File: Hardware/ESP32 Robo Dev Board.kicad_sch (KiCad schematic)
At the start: 44 parts, among them J2 Conn_01x02_Pin, Q1 DMP2045U, SW1 SW_Push_Dual_x2, U1 ESP32-S3-WROOM-1, U2 TCA9548ARGER, U8 MCP73831-2-OT, U9 AP2112K-3.3

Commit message: Tweaked n' fixed things with @Amoskeag
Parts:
- added Rs2: 18 KΩ, Resistor_SMD:R_0603_1608Metric, symbol Device:R_Small
- added Rs3: 100, Resistor_SMD:R_0603_1608Metric, symbol Device:R_Small
- added SW2: SW_Push, Button_Switch_THT:SW_TH_Tactile_Omron_B3F-100x, symbol Switch:SW_Push
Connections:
- net +3V3: now also Rs3.2
- net Boot: now also Rs2.2, SW2.2
- net GND: now also Rs2.1
- new net: Rs3.1, SW2.1

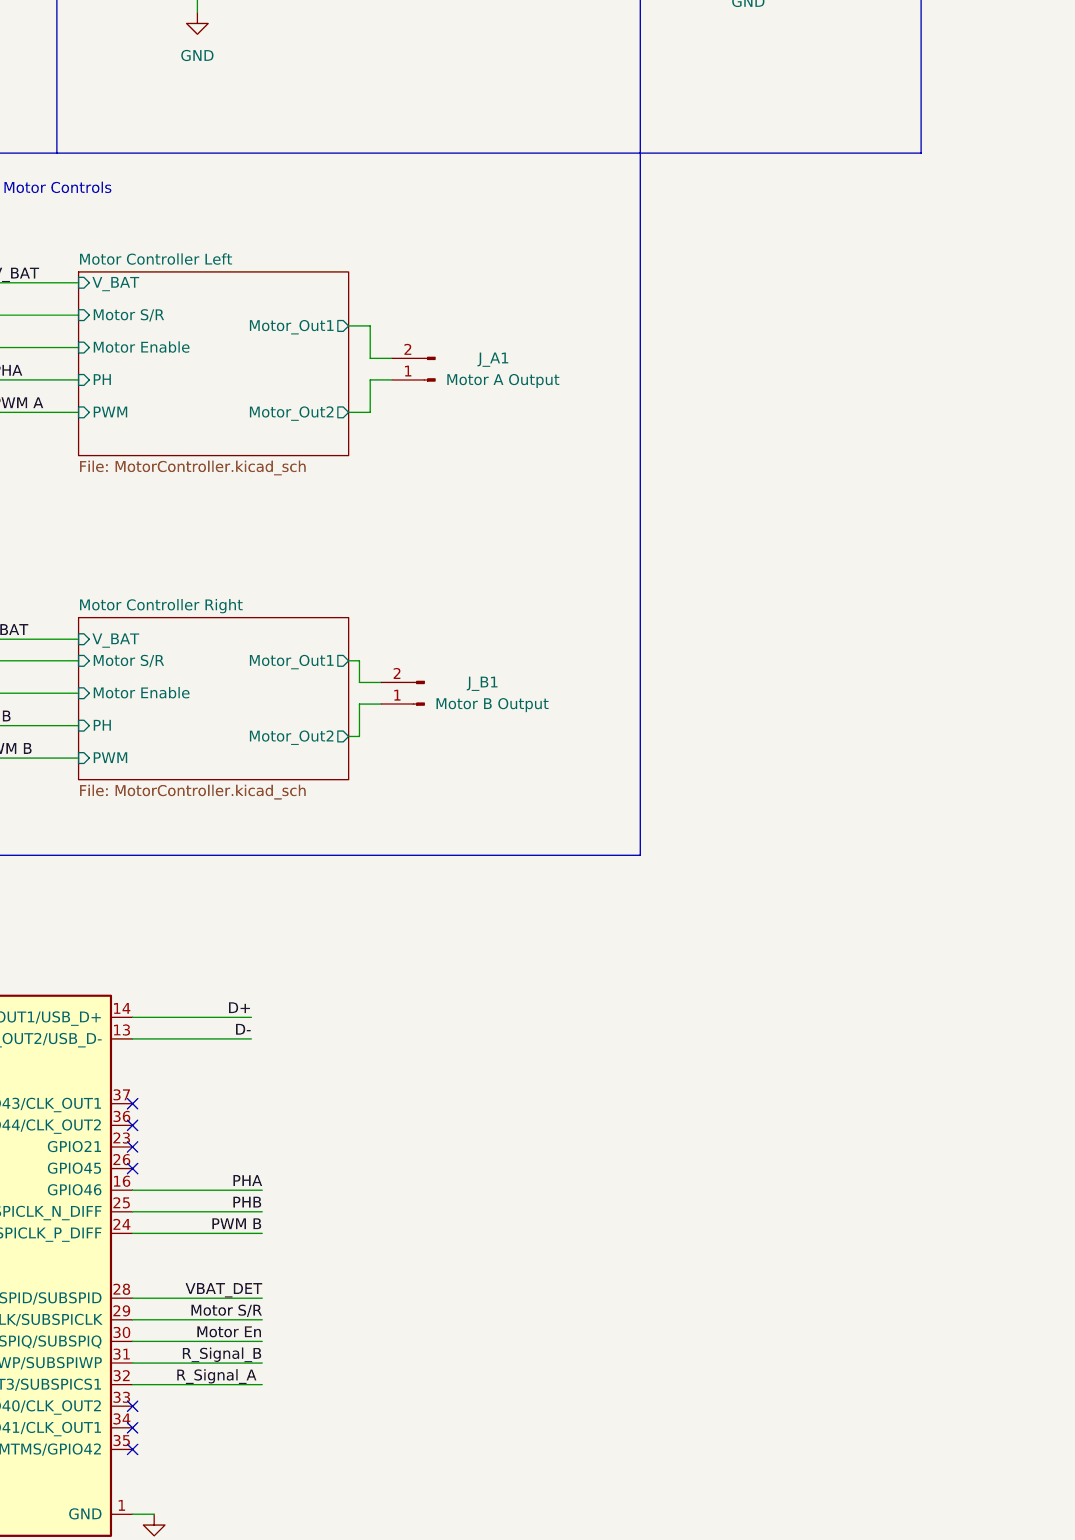
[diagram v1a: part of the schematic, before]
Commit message: Add JST Connectors for Encoders
Added JST Connectors for my Encoders to attach to.

Fixed all DRC Errors.
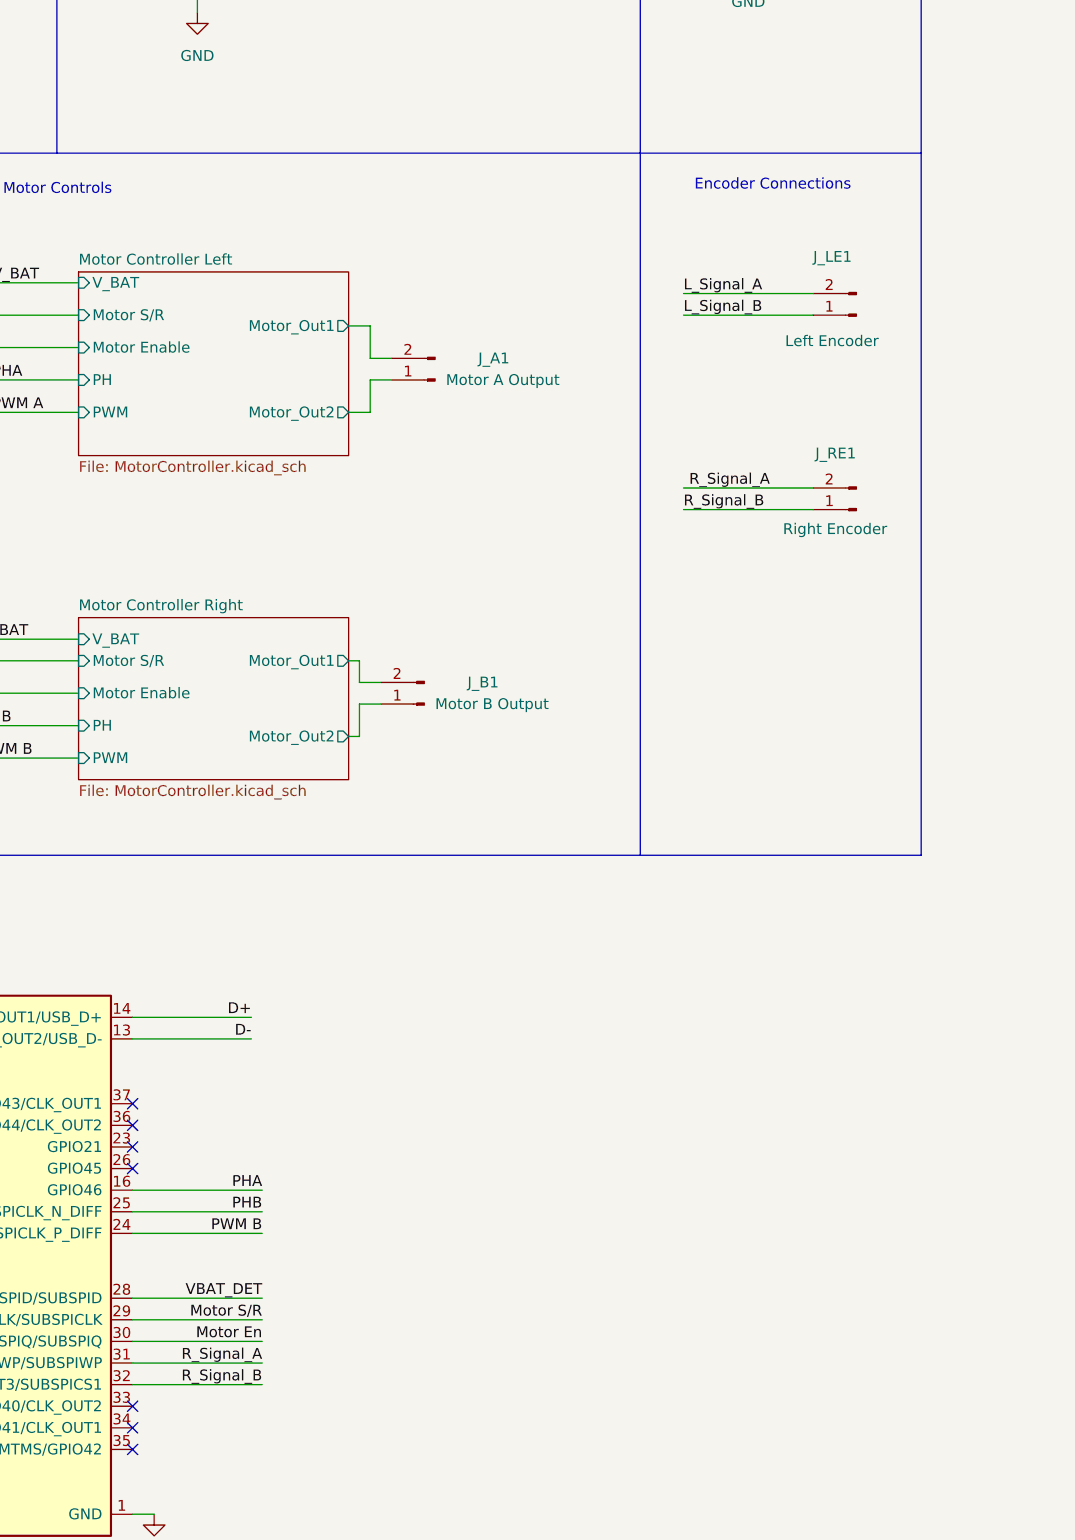
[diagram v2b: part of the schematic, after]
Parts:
- added J_LE1: Left Encoder, Connector_JST:JST_EH_B2B-EH-A_1x02_P2.50mm_Vertical, symbol Connector:Conn_01x02_Male
- added J_RE1: Right Encoder, Connector_JST:JST_EH_B2B-EH-A_1x02_P2.50mm_Vertical, symbol Connector:Conn_01x02_Male
- SW1: footprint Button_Switch_SMD:SW_Push_SPST_NO_Alps_SKRK -> Button_Switch_THT:SW_TH_Tactile_Omron_B3F-100x
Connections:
- net L_Signal_A: now also J_LE1.2 (Pin_2)
- net L_Signal_B: now also J_LE1.1 (Pin_1)
- net R_Signal_A: now also U1.31 (GPIO38/FSPIWP/SUBSPIWP), J_RE1.2 (Pin_2); no longer U1.32 (MTCK/GPIO39/CLK_OUT3/SUBSPICS1)
- net R_Signal_B: now also U1.32 (MTCK/GPIO39/CLK_OUT3/SUBSPICS1), J_RE1.1 (Pin_1); no longer U1.31 (GPIO38/FSPIWP/SUBSPIWP)
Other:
- note added: "Encoder Connections"
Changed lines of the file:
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@@
 		)
 	)
+	(text "Encoder Connections\n"
+		(exclude_from_sim no)
+		(at 322.58 82.042 0)
+		(effects
+			(font
+				(size 1.27 1.27)
+			)
+			(justify left bottom)
+		)
+	)
 	(text "Reset Circuts"
 		(exclude_from_sim no)
@@
 		)
 	)
+	(polyline
+		(pts
+			(xy 316.23 160.02) (xy 349.25 160.02)
+		)
+		(stroke
+			(width 0)
+			(type default)
+		)
+	)
 	(wire
 		(pts
@@
 		)
 	)
+	(polyline
+		(pts
+			(xy 349.25 77.47) (xy 349.25 160.02)
+		)
+		(stroke
+			(width 0)
+			(type default)
+		)
+	)
 	(wire
 		(pts
@@
 	(wire
 		(pts
-			(xy 256.54 222.25) (xy 271.78 222.25)
-		)
-		(stroke
-			(width 0)
-			(type default)
-		)
-	)
-	(wire
-		(pts
 			(xy 140.97 53.34) (xy 140.97 55.88)
 		)
@@
 	(wire
 		(pts
+			(xy 321.31 96.52) (xy 336.55 96.52)
+		)
+		(stroke
+			(width 0)
+			(type default)
+		)
+	)
+	(wire
+		(pts
 			(xy 26.67 114.3) (xy 21.59 114.3)
 		)
@@
 	(wire
 		(pts
+			(xy 336.55 116.84) (xy 321.31 116.84)
+		)
+		(stroke
+			(width 0)
+			(type default)
+		)
+	)
+	(wire
+		(pts
 			(xy 240.03 107.95) (xy 250.19 107.95)
 		)
@@
 	(wire
 		(pts
+			(xy 336.55 119.38) (xy 321.31 119.38)
+		)
+		(stroke
+			(width 0)
+			(type default)
+		)
+	)
+	(wire
+		(pts
 			(xy 57.15 90.17) (xy 58.42 90.17)
 		)
@@
 	(wire
 		(pts
-			(xy 256.54 199.39) (xy 271.78 199.39)
+			(xy 256.54 219.71) (xy 271.78 219.71)
 		)
 		(stroke
@@
 	(wire
 		(pts
-			(xy 147.32 127) (xy 166.37 127)
+			(xy 256.54 199.39) (xy 271.78 199.39)
 		)
 		(stroke
@@
 	(wire
 		(pts
-			(xy 284.48 104.14) (xy 287.02 104.14)
+			(xy 147.32 127) (xy 166.37 127)
 		)
 		(stroke
@@
 	(wire
 		(pts
-			(xy 267.97 46.99) (xy 267.97 57.15)
+			(xy 284.48 104.14) (xy 287.02 104.14)
 		)
 		(stroke
@@
 	(wire
 		(pts
-			(xy 127 217.17) (xy 142.24 217.17)
+			(xy 267.97 46.99) (xy 267.97 57.15)
 		)
 		(stroke
@@
 	(wire
 		(pts
-			(xy 256.54 219.71) (xy 271.78 219.71)
+			(xy 127 217.17) (xy 142.24 217.17)
 		)
 		(stroke
@@
 	(wire
 		(pts
+			(xy 256.54 222.25) (xy 271.78 222.25)
+		)
+		(stroke
+			(width 0)
+			(type default)
+		)
+	)
+	(wire
+		(pts
 			(xy 124.46 67.31) (xy 124.46 26.67)
 		)
@@
 	(wire
 		(pts
+			(xy 321.31 93.98) (xy 336.55 93.98)
+		)
+		(stroke
+			(width 0)
+			(type default)
+		)
+	)
+	(wire
+		(pts
 			(xy 82.55 156.21) (xy 80.01 156.21)
 		)
@@
 	)
 	(label "R_Signal_B"
-		(at 271.78 219.71 180)
+		(at 271.78 222.25 180)
 		(effects
 			(font
@@
 		)
 	)
+	(label "R_Signal_B"
+		(at 321.31 119.38 0)
+		(effects
+			(font
+				(size 1.27 1.27)
+			)
+			(justify left bottom)
+		)
+	)
 	(label "I2C_1D"
 		(at 156.21 106.68 180)
@@
 		)
 	)
+	(label "L_Signal_B"
+		(at 321.31 96.52 0)
+		(effects
+			(font
+				(size 1.27 1.27)
+			)
+			(justify left bottom)
+		)
+	)
 	(label "I2C_5C"
 		(at 82.55 111.76 180)
@@
 		)
 	)
+	(label "R_Signal_A"
+		(at 331.47 116.84 180)
+		(effects
+			(font
+				(size 1.27 1.27)
+			)
+			(justify right bottom)
+		)
+	)
 	(label "I2C_3C"
 		(at 60.96 158.75 180)
@@
 		)
 	)
+	(label "L_Signal_A"
+		(at 321.31 93.98 0)
+		(effects
+			(font
+				(size 1.27 1.27)
+			)
+			(justify left bottom)
+		)
+	)
 	(label "V_IN"
 		(at 50.8 40.64 0)
@@
 	)
 	(label "R_Signal_A"
-		(at 261.62 222.25 0)
+		(at 271.78 219.71 180)
 		(effects
 			(font
 				(size 1.27 1.27)
 			)
-			(justify left bottom)
+			(justify right bottom)
 		)
 	)
@@
 	)
 	(symbol
+		(lib_id "Connector:Conn_01x02_Male")
+		(at 341.63 96.52 180)
+		(unit 1)
+		(exclude_from_sim no)
+		(in_bom yes)
+		(on_board yes)
+		(dnp no)
+		(property "Reference" "J_LE1"
+			(at 336.55 89.662 0)
+			(effects
+				(font
+					(size 1.27 1.27)
+				)
+				(justify right)
+			)
+		)
+		(property "Value" "Left Encoder"
+			(at 333.248 99.568 0)
+			(effects
+				(font
+					(size 1.27 1.27)
+				)
+				(justify right)
+			)
+		)
+		(property "Footprint" "Connector_JST:JST_EH_B2B-EH-A_1x02_P2.50mm_Vertical"
+			(at 341.63 96.52 0)
+			(effects
+				(font
+					(size 1.27 1.27)
+				)
+				(hide yes)
+			)
+		)
+		(property "Datasheet" "~"
+			(at 341.63 96.52 0)
+			(effects
+				(font
+					(size 1.27 1.27)
+				)
+				(hide yes)
+			)
+		)
+		(property "Description" ""
+			(at 341.63 96.52 0)
+			(effects
+				(font
+					(size 1.27 1.27)
+				)
+				(hide yes)
+			)
+		)
+		(pin "1"
+		)
+		(pin "2"
+		)
+		(instances
+			(project "ESP32 Robo Dev Board"
+				(path "/e63e39d7-6ac0-4ffd-8aa3-1841a4541b55"
+					(reference "J_LE1")
+					(unit 1)
+				)
+			)
+		)
+	)
+	(symbol
 		(lib_id "power:GND")
 		(at 88.9 207.01 0)
@@
 	)
 	(symbol
+		(lib_id "Connector:Conn_01x02_Male")
+		(at 341.63 119.38 180)
+		(unit 1)
+		(exclude_from_sim no)
+		(in_bom yes)
+		(on_board yes)
+		(dnp no)
+		(property "Reference" "J_RE1"
+			(at 336.804 112.776 0)
+			(effects
+				(font
+					(size 1.27 1.27)
+				)
+				(justify right)
+			)
+		)
+		(property "Value" "Right Encoder"
+			(at 332.994 121.666 0)
+			(effects
+				(font
+					(size 1.27 1.27)
+				)
+				(justify right)
+			)
+		)
+		(property "Footprint" "Connector_JST:JST_EH_B2B-EH-A_1x02_P2.50mm_Vertical"
+			(at 341.63 119.38 0)
+			(effects
+				(font
+					(size 1.27 1.27)
+				)
+				(hide yes)
+			)
+		)
+		(property "Datasheet" "~"
+			(at 341.63 119.38 0)
+			(effects
+				(font
+					(size 1.27 1.27)
+				)
+				(hide yes)
+			)
+		)
+		(property "Description" ""
+			(at 341.63 119.38 0)
+			(effects
+				(font
+					(size 1.27 1.27)
+				)
+				(hide yes)
+			)
+		)
+		(pin "1"
+		)
+		(pin "2"
+		)
+		(instances
+			(project "ESP32 Robo Dev Board"
+				(path "/e63e39d7-6ac0-4ffd-8aa3-1841a4541b55"
+					(reference "J_RE1")
+					(unit 1)
+				)
+			)
+		)
+	)
+	(symbol
 		(lib_id "Device:R_Small")
 		(at 220.98 49.53 0)
@@
 			)
 		)
-		(property "Footprint" "Button_Switch_SMD:SW_Push_SPST_NO_Alps_SKRK"
+		(property "Footprint" "Button_Switch_THT:SW_TH_Tactile_Omron_B3F-100x"
 			(at 254 44.45 0)
 			(effects

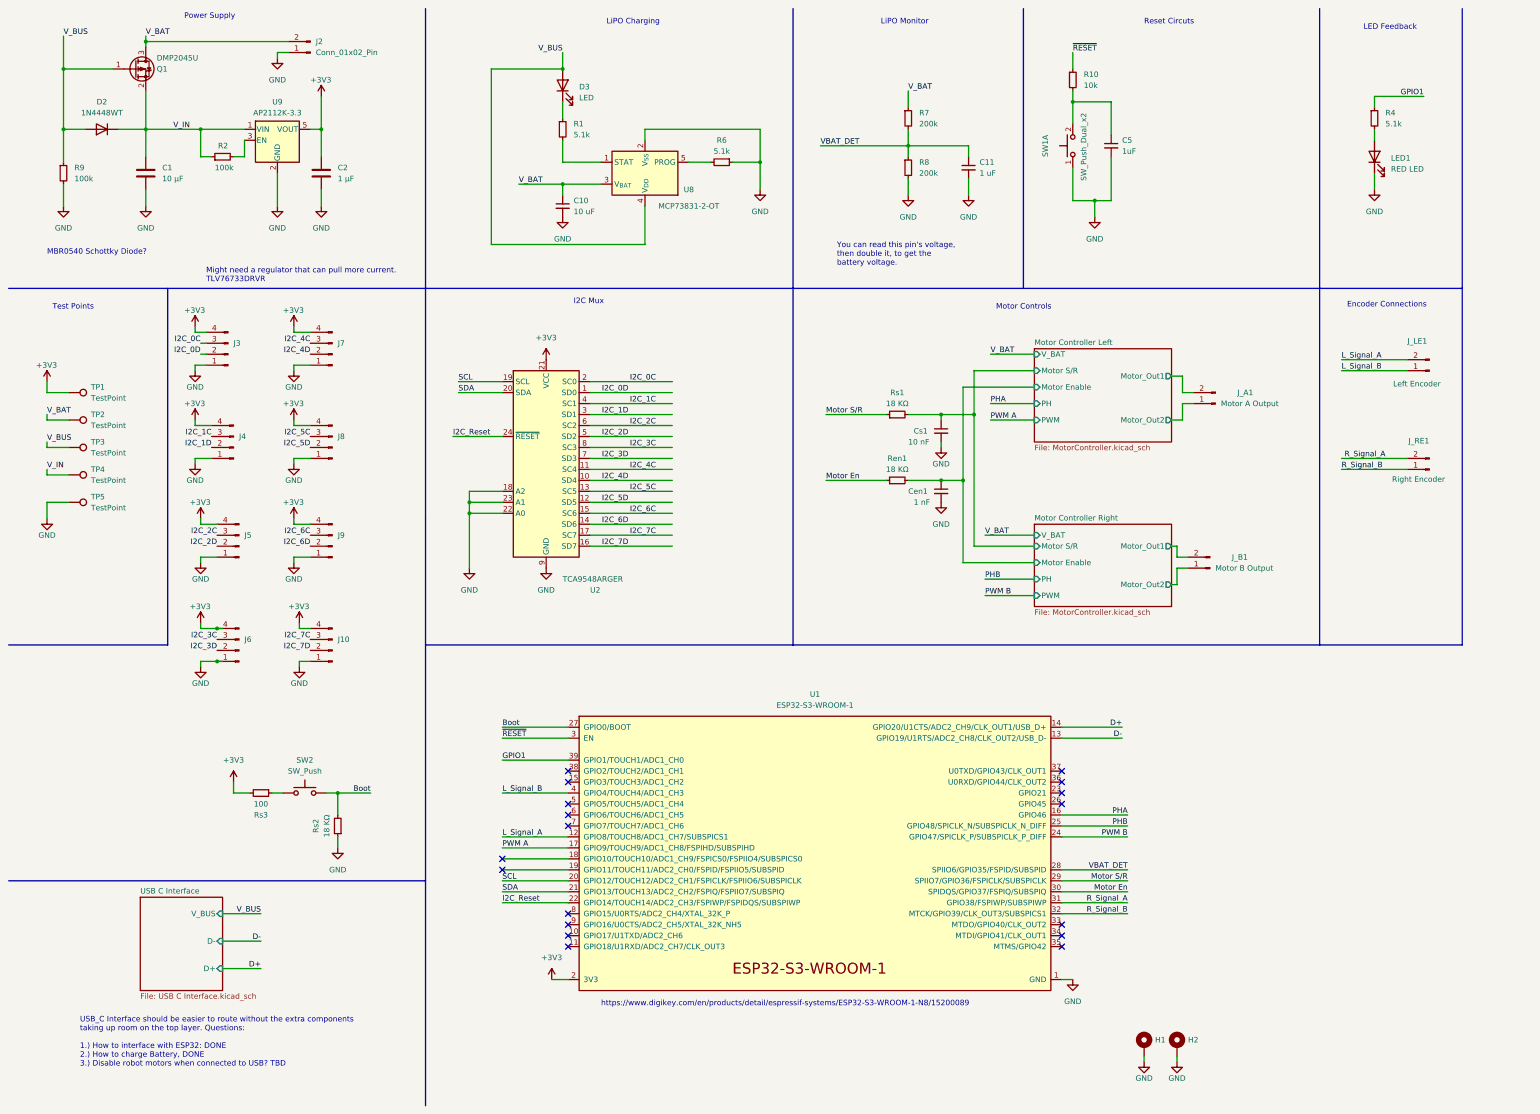
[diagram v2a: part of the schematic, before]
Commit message: Clean Up Schematic
Fixed Schematic notes, and formatting
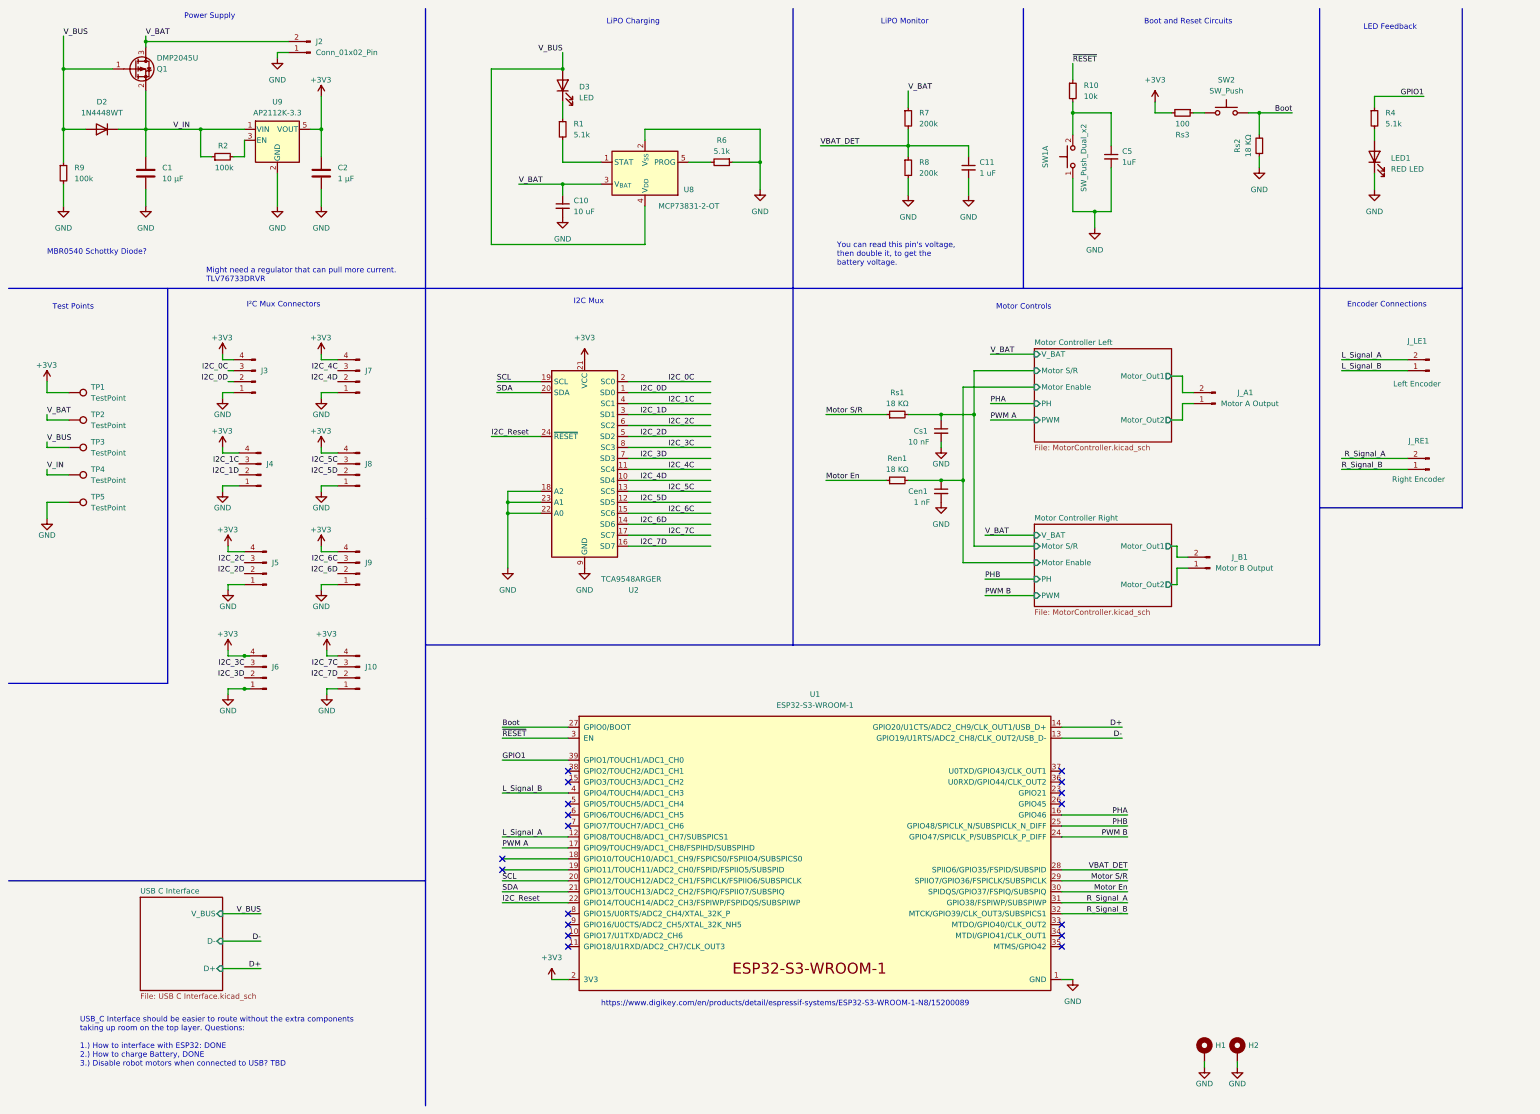
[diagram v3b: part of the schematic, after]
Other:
- note added: "Boot and Reset Circuits"
- note added: "I²C Mux Connectors"
- note removed: "Reset Circuts"
- moved on the sheet: C5, H1, H2, J10, J3, J4, J5, J6, J7, J8, J9, R10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
